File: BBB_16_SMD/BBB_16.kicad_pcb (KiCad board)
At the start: 2 copper layers, 148.8 x 116.9 mm, 114 parts, among them J1 String1, J10 String10, J11 String11, J12 String12, J13 String13, J14 String14, J15 String15, J16 String16, J17 Power In Left, J18 Power In Right, J19 GPIO, J2 String2, J20 DMX1 RJ45, J21 RJ45, J22 DMX2, J23 VIN Voltage, J24 Expansion Header, J25 RTC Conn, J26 OLED, J27 Aux Pwr, J28 VIN Select, J3 String3, J4 String4, J5 String5, J6 String6, J7 String7, J8 String8, J9 String9, Q1 DMP3056L, SW1 Left BTN, SW2 Up BTN, SW3 Down BTN, SW4 Right BTN, SW5 PWR BTN, SW6 DMX_LOR_Select, U1 BEAGLEBONEBLACK, U2 LM7805, U3 SN74HCT245N, U4 SN74HCT245N, U5 UA9638CP, U6 24L256, U7 AM26C31

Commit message: added logo
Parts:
- added G***: LOGO, Scotts:chewi_15, F.Cu at (127.5, 59.7)

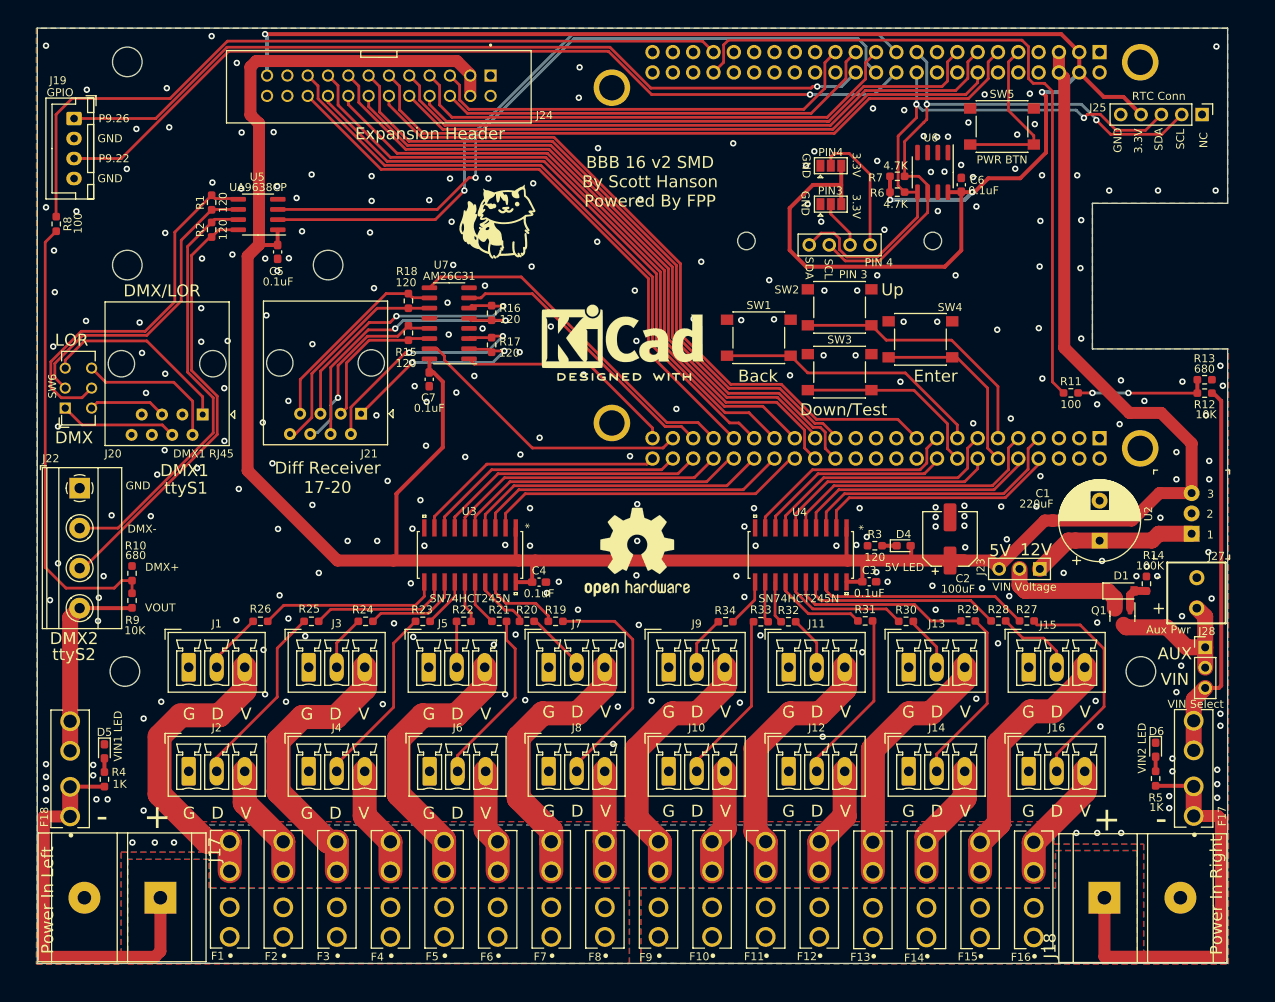
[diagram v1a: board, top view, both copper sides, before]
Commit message: Small updates
Update Wrong switch that would force standard pcb vs Economic variant. Update Rj45 PartNumber.
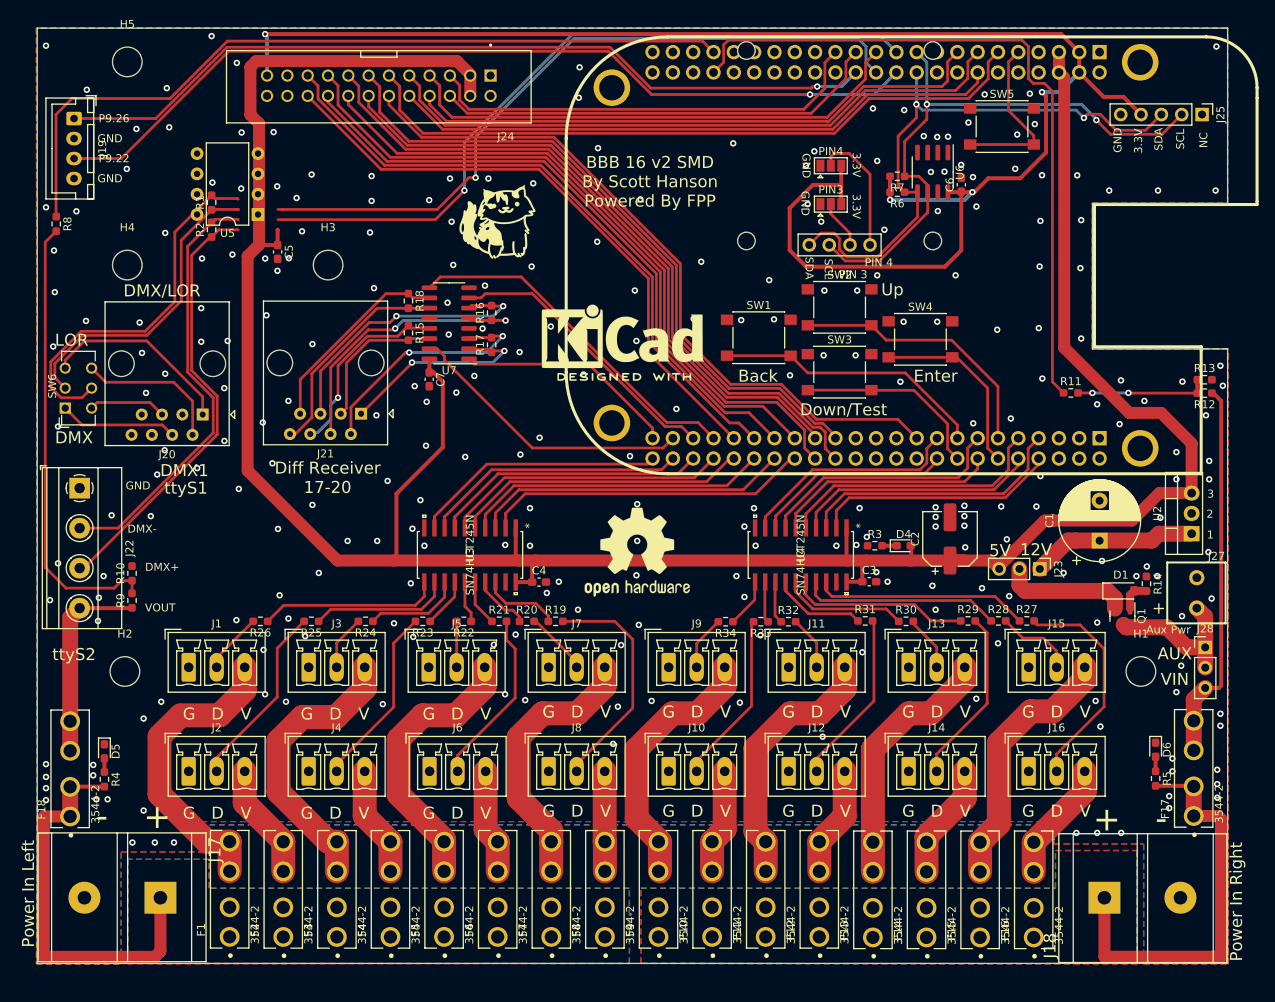
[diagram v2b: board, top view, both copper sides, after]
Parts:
- U2: footprint OKI-78SR-5:SIP-3_P2.54mm_OKI-78SR-5_1.5-W36-C -> Package_TO_SOT_THT:TO-220-3_Vertical
- U5: footprint Package_SO:SOIC-8_3.9x4.9mm_P1.27mm -> Package_DIP:DIP-8_W7.62mm
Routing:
- net /Serial/DMX1+: track 39.0 -> 0.00 mm
- net /Serial/DMX1-: track 46.7 -> 85.7 mm

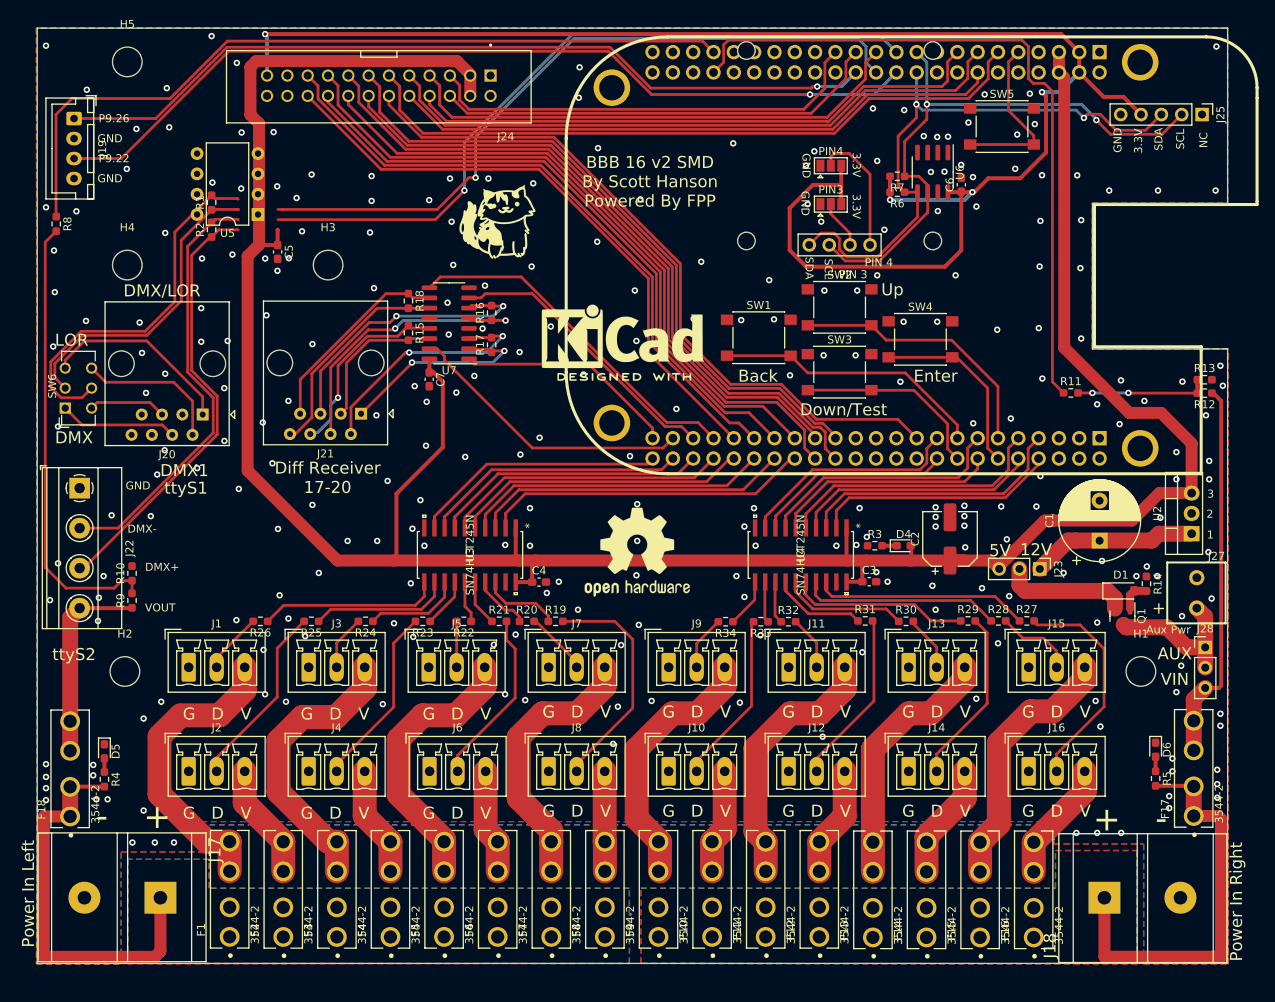
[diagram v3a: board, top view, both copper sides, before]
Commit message: reverting bills change
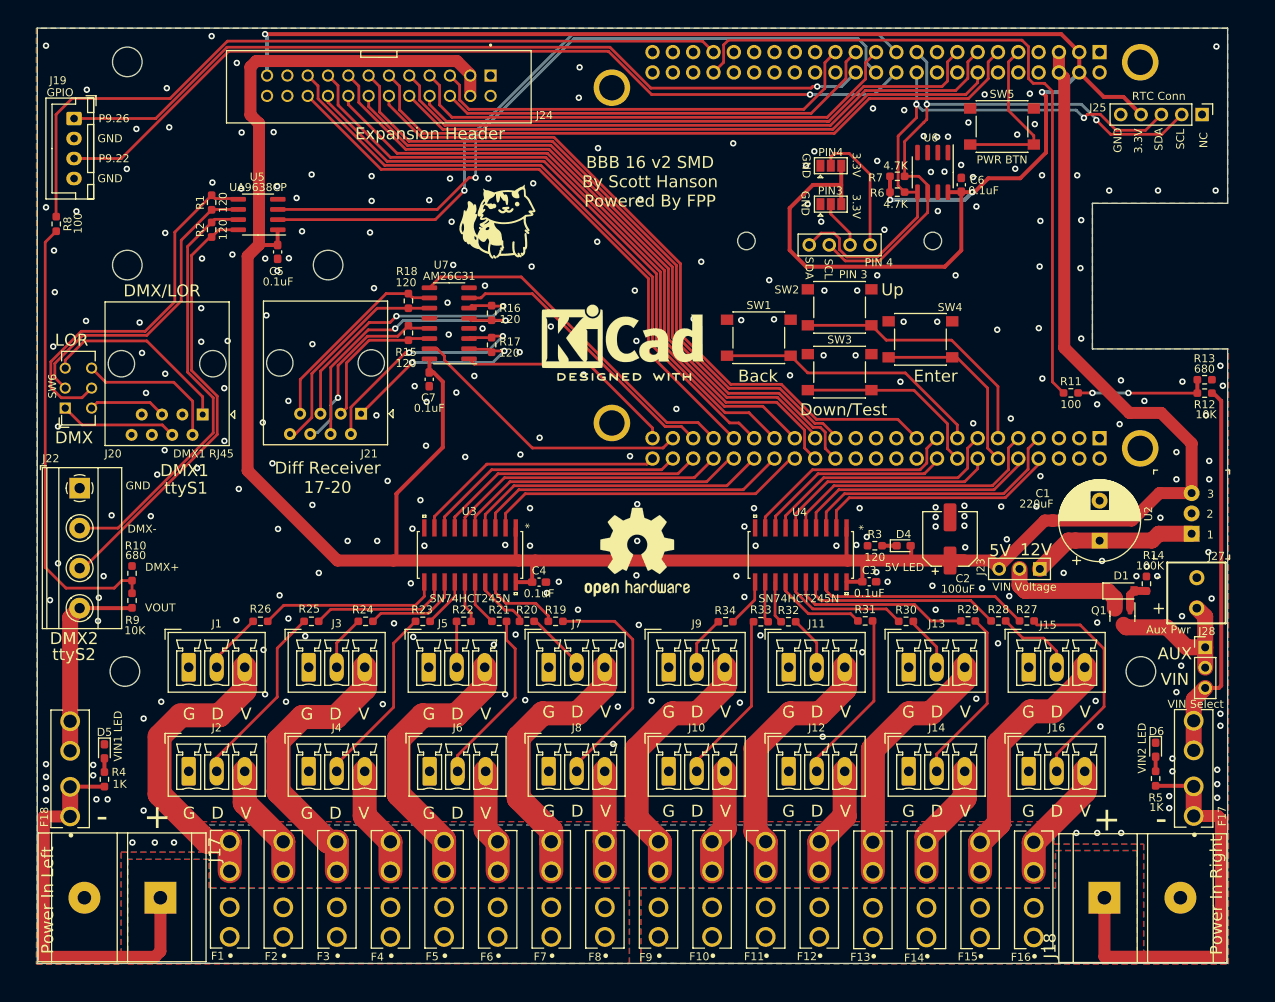
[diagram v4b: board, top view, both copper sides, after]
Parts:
- U2: footprint Package_TO_SOT_THT:TO-220-3_Vertical -> OKI-78SR-5:SIP-3_P2.54mm_OKI-78SR-5_1.5-W36-C
- U5: footprint Package_DIP:DIP-8_W7.62mm -> Package_SO:SOIC-8_3.9x4.9mm_P1.27mm
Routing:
- net /Serial/DMX1+: track 0.00 -> 39.0 mm
- net /Serial/DMX1-: track 85.7 -> 46.7 mm
